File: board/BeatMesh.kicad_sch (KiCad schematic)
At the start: 70 parts, among them J1 AudioJack3_SwitchTR, J10 AudioJack3_SwitchTR, J12 DIN-5_180degree, J13 USB_C_Receptacle_USB2.0_16P, J14 Conn_01x04_Pin, J15 Conn_01x02, J16 Conn_01x02, J17 AudioJack3_SwitchTR, J18 AudioJack3_SwitchTR, J19 Conn_01x06_Pin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

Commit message: errata V1 + updated to kicad 10
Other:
- note added: "TODO: next version should use a friendly part: HRO TYPE-C-31-M-12"
- note added: "TODO: switch to TO-92_Wide"

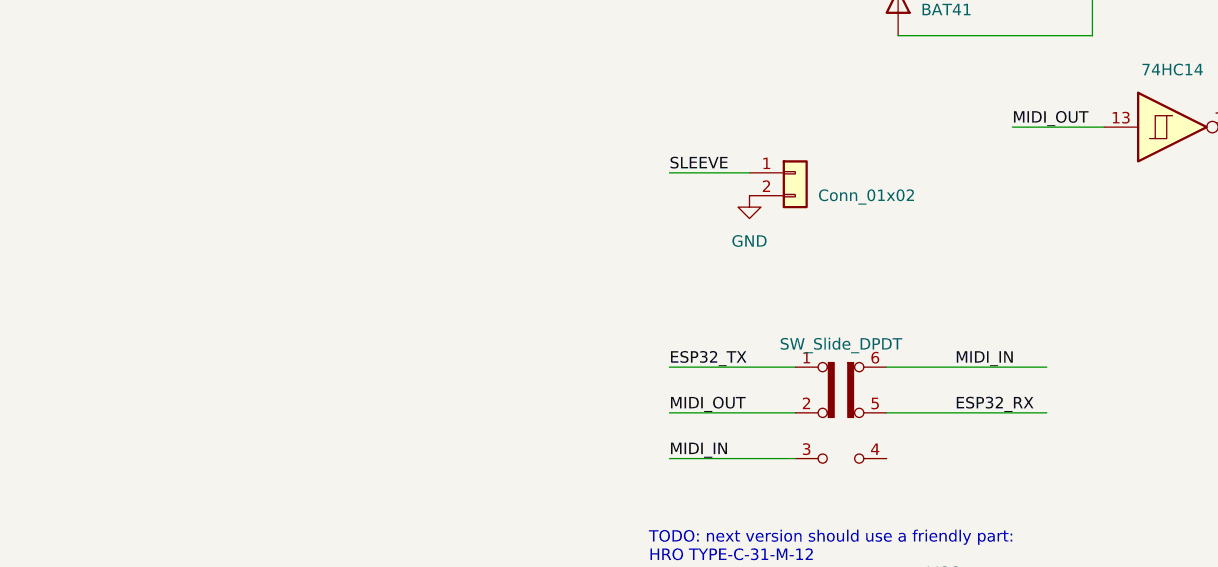
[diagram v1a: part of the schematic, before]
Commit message: modulo for ppqn, added TODO in pcb
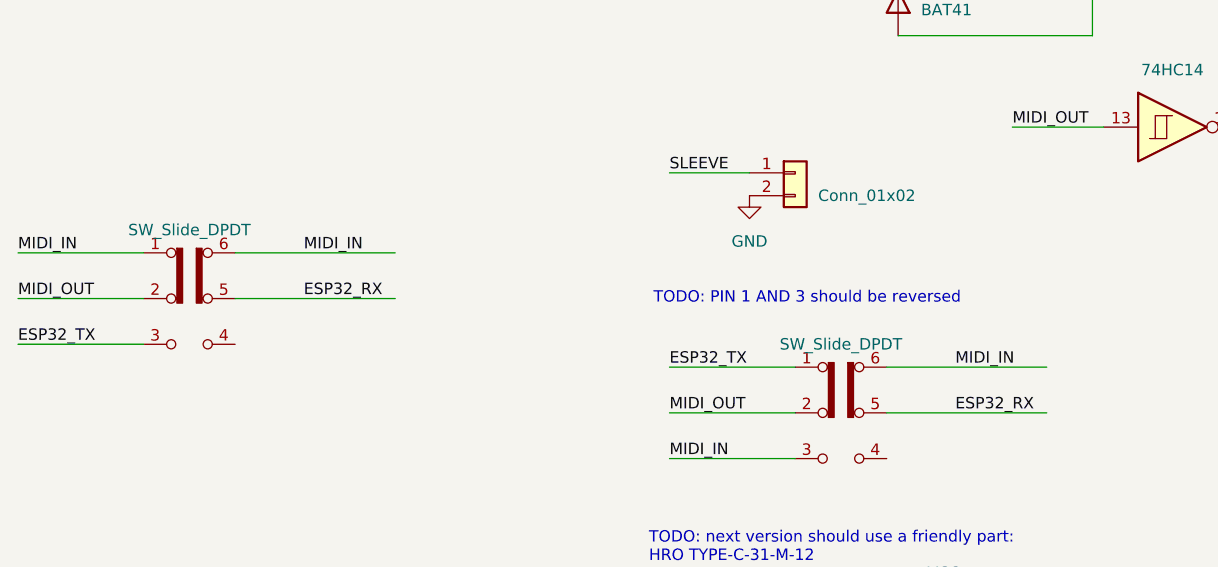
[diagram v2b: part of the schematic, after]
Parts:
- added SW2: SW_Slide_DPDT, Button_Switch_THT:SW_E-Switch_EG2219_DPDT_Angled, symbol Switch:SW_Slide_DPDT
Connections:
- net ESP32_RX: now also SW2.5 (B)
- net ESP32_TX: now also SW2.3 (C)
- net MIDI_IN: now also SW2.1 (A), SW2.6 (C)
- net MIDI_OUT: now also SW2.2 (B)
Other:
- note added: "TODO: PIN 1 AND 3 should be reversed"
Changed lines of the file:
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@@
 		)
 	)
+	(text "TODO: PIN 1 AND 3 should be reversed"
+		(exclude_from_sim no)
+		(at 18.542 90.17 0)
+		(effects
+			(font
+				(size 1.27 1.27)
+				(color 255 141 0 1)
+			)
+			(justify left)
+		)
+	)
 	(junction
 		(at 195.58 45.72)
@@
 	(wire
 		(pts
+			(xy -27.94 90.17) (xy -10.16 90.17)
+		)
+		(stroke
+			(width 0)
+			(type default)
+		)
+	)
+	(wire
+		(pts
 			(xy 148.59 189.23) (xy 158.75 189.23)
 		)
@@
 	(wire
 		(pts
+			(xy -52.07 85.09) (xy -38.1 85.09)
+		)
+		(stroke
+			(width 0)
+			(type default)
+		)
+	)
+	(wire
+		(pts
 			(xy 67.31 60.96) (xy 67.31 39.37)
 		)
@@
 	(wire
 		(pts
+			(xy -27.94 85.09) (xy -10.16 85.09)
+		)
+		(stroke
+			(width 0)
+			(type default)
+		)
+	)
+	(wire
+		(pts
 			(xy 127 26.67) (xy 127 33.02)
 		)
@@
 	(wire
 		(pts
+			(xy -52.07 90.17) (xy -38.1 90.17)
+		)
+		(stroke
+			(width 0)
+			(type default)
+		)
+	)
+	(wire
+		(pts
 			(xy 193.04 85.09) (xy 199.39 85.09)
 		)
@@
 	(wire
 		(pts
+			(xy -52.07 95.25) (xy -38.1 95.25)
+		)
+		(stroke
+			(width 0)
+			(type default)
+		)
+	)
+	(wire
+		(pts
 			(xy 120.65 149.86) (xy 129.54 149.86)
 		)
@@
 		)
 	)
+	(label "MIDI_OUT"
+		(at -52.07 90.17 0)
+		(effects
+			(font
+				(size 1.27 1.27)
+			)
+			(justify left bottom)
+		)
+	)
 	(label "IO27_CV_PLAYSTOP"
 		(at 217.17 134.62 0)
@@
 		)
 	)
+	(label "MIDI_IN"
+		(at -52.07 85.09 0)
+		(effects
+			(font
+				(size 1.27 1.27)
+			)
+			(justify left bottom)
+		)
+	)
 	(label "ESP32_3.3V"
 		(at 196.85 36.83 0)
@@
 		)
 	)
+	(label "ESP32_RX"
+		(at -20.32 90.17 0)
+		(effects
+			(font
+				(size 1.27 1.27)
+			)
+			(justify left bottom)
+		)
+	)
 	(label "IO35"
 		(at 203.2 45.72 0)
@@
 		)
 	)
+	(label "MIDI_IN"
+		(at -20.32 85.09 0)
+		(effects
+			(font
+				(size 1.27 1.27)
+			)
+			(justify left bottom)
+		)
+	)
 	(label "SLEEVE"
 		(at 121.92 133.35 0)
@@
 		)
 	)
+	(label "ESP32_TX"
+		(at -52.07 95.25 0)
+		(effects
+			(font
+				(size 1.27 1.27)
+			)
+			(justify left bottom)
+		)
+	)
 	(label "IO35"
 		(at 262.89 38.1 0)
@@
 					(unit 1)
 				)
+			)
+		)
+	)
+	(symbol
+		(lib_id "Switch:SW_Slide_DPDT")
+		(at -33.02 90.17 0)
+		(unit 1)
+		(body_style 1)
+		(exclude_from_sim no)
+		(in_bom yes)
+		(on_board yes)
+		(in_pos_files yes)
+		(dnp no)
+		(fields_autoplaced yes)
+		(property "Reference" "SW2"
+			(at -33.02 80.01 0)
+			(hide yes)
+			(show_name no)
+			(do_not_autoplace no)
+			(effects
+				(font
+					(size 1.27 1.27)
+				)
+			)
+		)
+		(property "Value" "SW_Slide_DPDT"
+			(at -33.02 82.55 0)
+			(show_name no)
+			(do_not_autoplace no)
+			(effects
+				(font
+					(size 1.27 1.27)
+				)
+			)
+		)
+		(property "Footprint" "Button_Switch_THT:SW_E-Switch_EG2219_DPDT_Angled"
+			(at -19.05 85.09 0)
+			(hide yes)
+			(show_name no)
+			(do_not_autoplace no)
+			(effects
+				(font
+					(size 1.27 1.27)
+				)
+			)
+		)
+		(property "Datasheet" ""
+			(at -33.02 90.17 0)
+			(hide yes)
+			(show_name no)
+			(do_not_autoplace no)
+			(effects
+				(font
+					(size 1.27 1.27)
+				)
+			)
+		)
+		(property "Description" "Slide Switch, dual pole double throw"
+			(at -33.02 90.17 0)
+			(hide yes)
+			(show_name no)
+			(do_not_autoplace no)
+			(effects
+				(font
+					(size 1.27 1.27)
+				)
+			)
+		)
+		(pin "4"
+		)
+		(pin "5"
+		)
+		(pin "2"
+		)
+		(pin "6"
+		)
+		(pin "3"
+		)
+		(pin "1"
+		)
+		(instances
+			(project "BeatMesh"
+				(path "/14ea9578-4898-4ef4-b762-ae0714ccfadc"
+					(reference "SW2")
+					(unit 1)
+				)

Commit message: notes on pins
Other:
- note added: "io21 do not use, so we loose start-stop"
- note added: "play - stop is now reset"
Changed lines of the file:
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@@
+		)
+	)
+	(text "play - stop is now reset"
+		(exclude_from_sim no)
+		(at 294.386 34.544 0)
+		(effects
+			(font
+				(size 1.27 1.27)
+			)
+		)
+	)
+	(text "io21 do not use, so we loose start-stop"
+		(exclude_from_sim no)
+		(at 300.228 29.464 0)
+		(effects
+			(font
+				(size 1.27 1.27)
+			)
 		)
 	)

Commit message: board v2
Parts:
- removed J18: AudioJack3_SwitchTR, Connector_Audio:Jack_3.5mm_CUI_SJ1-3515N_Horizontal, symbol Connector_Audio:AudioJack3_SwitchTR
- removed J19: Conn_01x06_Pin, Connector_PinHeader_2.54mm:PinHeader_1x06_P2.54mm_Vertical, symbol Connector:Conn_01x06_Pin
- removed R27: 1K, Resistor_THT:R_Axial_DIN0204_L3.6mm_D1.6mm_P5.08mm_Horizontal, symbol Device:R
- removed SW2: SW_Slide_DPDT, Button_Switch_THT:SW_E-Switch_EG2219_DPDT_Angled, symbol Switch:SW_Slide_DPDT
- removed unit 3 of U4
- added J11: Conn_01x05_Pin, Connector_PinHeader_2.54mm:PinHeader_1x05_P2.54mm_Vertical, symbol Connector:Conn_01x05_Pin
- J13: footprint Connector_USB:USB_C_Receptacle_GCT_USB4085 -> Connector_USB:USB_C_Receptacle_HRO_TYPE-C-31-M-12
- Q1: footprint Package_TO_SOT_THT:TO-92_Inline -> Package_TO_SOT_THT:TO-92_Inline_Wide
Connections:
- net ESP32_3.3V: now also J11.1 (Pin_1)
- net ESP32_TX: now also SW1.3 (C); no longer SW1.1 (A)
- net GND: now also J11.5 (Pin_5)
- net IO22_CV_CLOCK: now also J11.2 (Pin_2)
- net IO35: now also J11.4 (Pin_4)
- net MIDI_IN: now also SW1.1 (A); no longer SW1.3 (C)
- new net IO27_CV_RESET: J11.3 (Pin_3)
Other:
- note added: "CV OUT CLOCK, RESET"
- note removed: "CV CLOCK, RESET, START-STOP OUT"
- note removed: "TODO: PIN 1 AND 3 should be reversed"
- note removed: "TODO: next version should use a friendly part: HRO TYPE-C-31-M-12"
- note removed: "TODO: switch to TO-92_Wide"
- note removed: "io21 do not use, so we loose start-stop"
- note removed: "play - stop is now reset"
